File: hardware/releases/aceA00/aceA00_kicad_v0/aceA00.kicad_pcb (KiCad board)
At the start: 2 copper layers, 24.1 x 46.7 mm, 28 parts, among them J1 Conn_01x08_Socket, J10 Conn_01x08_Pin, J2 Conn_01x08_Pin, J3 Conn_01x02_Socket, J4 Conn_01x08_Pin, J5 Conn_01x08_Pin, J6 Conn_01x08_Socket, J7 Conn_01x08_Pin, J8 Conn_01x02_Socket, J9 Conn_01x08_Pin

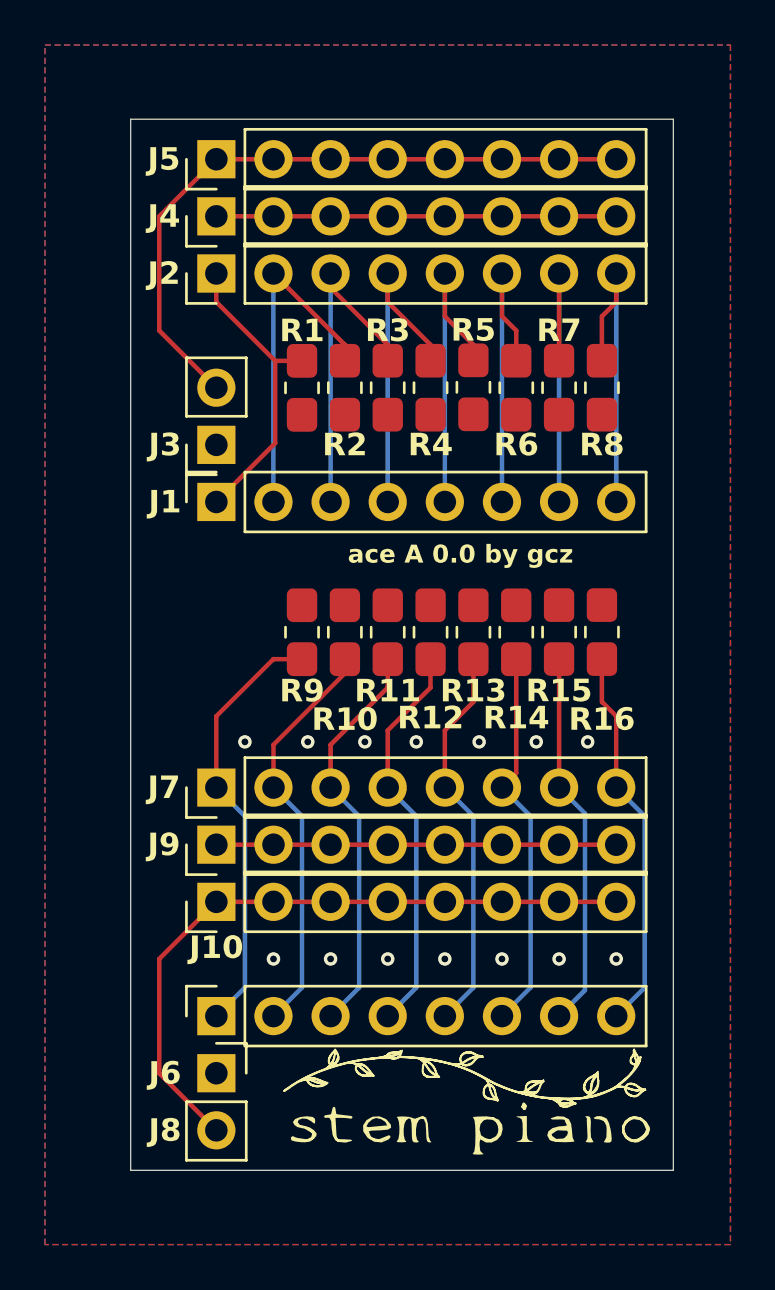
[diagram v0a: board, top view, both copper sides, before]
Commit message: moving connectors for IPS on the bottom of the ACE board, per issue #70
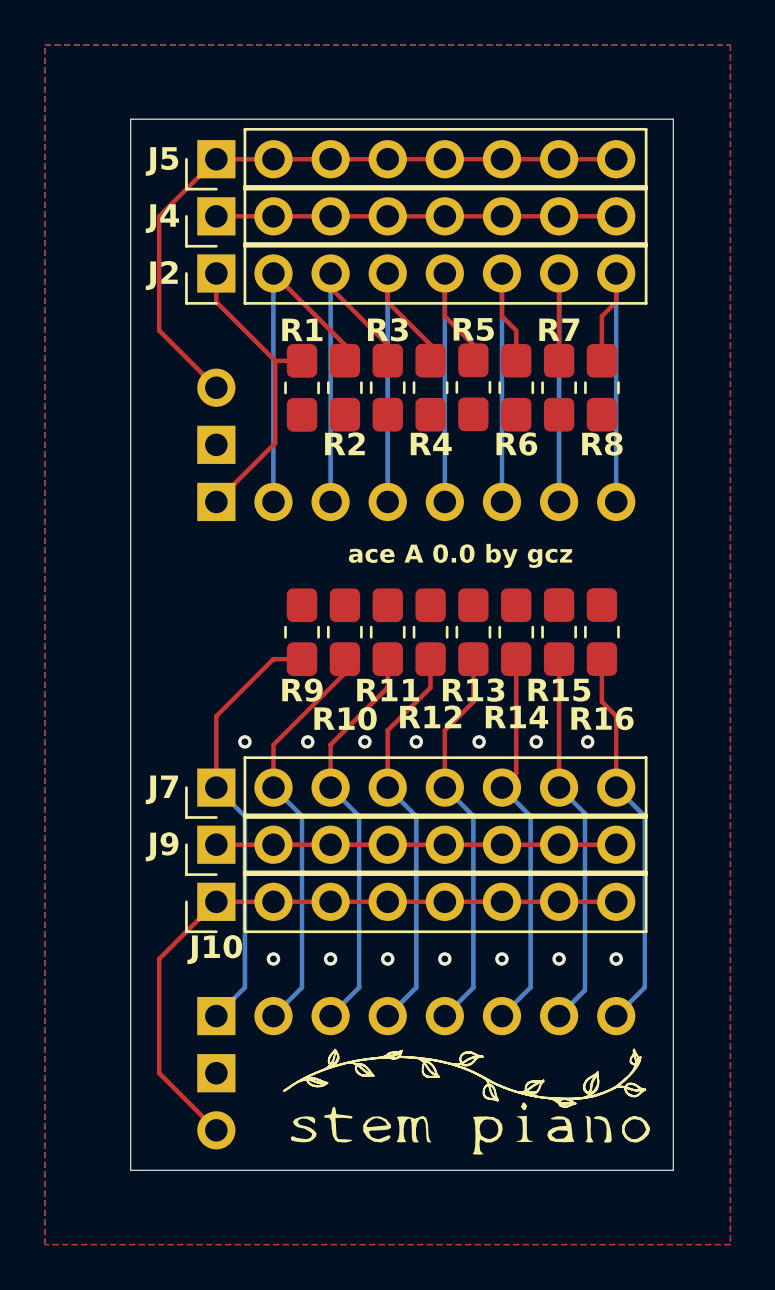
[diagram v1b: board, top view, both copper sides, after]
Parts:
- J1, J3, J6, J8: moved to B.Cu
- turned J1 to -90 degrees
- turned J3 to 0 degrees
- turned J6 to -90 degrees
- turned J8 to 180 degrees
